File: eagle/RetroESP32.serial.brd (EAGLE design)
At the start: 71.2 x 115 mm, 70 parts, among them J1 AUDIO_JACK_3.5MM_KIT, J2 SPKR, J3 Batt Conn, J5 503182-1852_503182-1852, J6 USB4110-GF-A, Q3 DMG3415U-7, Q4 mmbt2222, Q5 mmbt2222, U1 ESP32-WROVER_ESP32-WROVER, U3 XC6210B332MR-G, U4 MCP73832T-2ACI/OT, U6 LM4875

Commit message: chore: pre indiegogo commit
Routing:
- net 3V3: track 299.7 -> 281.1 mm
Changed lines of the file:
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@@
 <drawing>
 <settings>
-<setting alwaysvectorfont="no"/>
+<setting alwaysvectorfont="yes"/>
 <setting verticaltext="up"/>
 </settings>
-<grid distance="1" unitdist="mm" unit="mm" style="lines" multiple="1" display="yes" altdistance="0.5" altunitdist="mm" altunit="mm"/>
+<grid distance="1" unitdist="mm" unit="mm" style="lines" multiple="1" display="yes" altdistance="0.05" altunitdist="mm" altunit="mm"/>
 <layers>
 <layer number="1" name="Top" color="4" fill="1" visible="yes" active="yes"/>
@@
 </layers>
 <board>
-<fusionsync huburn="a.cGVyc29uYWw6dWUyYjExYjI4" projecturn="a.cGVyc29uYWw6dWUyYjExYjI4IzIwMTkwNjA2MTk3NjIxNDMx" f3durn="urn:adsk.wipprod:dm.lineage:ZFl1xGfIQ26tyrlassmjWg" pcbguid="b66a3f17-6c90-49ae-b368-ab31643a6c6c" lastpulledtime="" lastsyncedchangeguid="1d1d8de5-610f-f58b-7720-f87a5a059bbd" latestrevisionid="" lastsyncedrevisionid="" lastboardhashguid="38cdb7cc-8c8c-2878-219a-16e2d022a318" lastpushedtime="2021-09-21T20:27:47Z" linktopcb3d="false"/>
 <fusionteam huburn="a.cGVyc29uYWw6dWUyYjExYjI4" projecturn="a.cGVyc29uYWw6dWUyYjExYjI4IzIwMTkwNjA2MTk3NjIxNDMx" folderUrn="urn:adsk.wipprod:fs.folder:co.pA_OyOrURcuKuaZfHTjB4g" urn="urn:adsk.wipprod:dm.lineage:ZdROvaXvSf-QMBwcavZMUg"  versionUrn="urn:adsk.wipprod:fs.file:vf.ZdROvaXvSf-QMBwcavZMUg?version=2" camFileUrn="urn:adsk.wipprod:dm.lineage:iU1Nsl3HQ2WKUaZAR9U5UA" camFileVersionUrn="urn:adsk.wipprod:fs.file:vf.iU1Nsl3HQ2WKUaZAR9U5UA?version=2" lastpublishedchangeguid="9850a083-763b-e2cf-a501-3ff3fee0d740"/>
 <plain>
@@
 <text x="2.1" y="31" size="1.016" layer="26" font="vector" ratio="20" rot="MR270" align="center">SCREW</text>
 <text x="2.1" y="27" size="1.4224" layer="26" font="vector" ratio="12" rot="SMR180" align="center">⇪</text>
-<polygon width="0" layer="21">
-<vertex x="0" y="52"/>
-<vertex x="0" y="1" curve="90"/>
-<vertex x="1" y="0"/>
-<vertex x="1" y="-0.5"/>
-<vertex x="17" y="-0.5"/>
-<vertex x="17" y="0"/>
-<vertex x="35" y="0" curve="90"/>
-<vertex x="35.5" y="0.5"/>
-<vertex x="35.5" y="1.75"/>
-<vertex x="42.5" y="1.75"/>
-<vertex x="42.5" y="0.5" curve="90"/>
-<vertex x="43" y="0"/>
-<vertex x="49.5" y="0" curve="90"/>
-<vertex x="50.5" y="1"/>
-<vertex x="50.5" y="16.95"/>
-<vertex x="68.5" y="16.95" curve="90"/>
-<vertex x="69.5" y="17.95"/>
-<vertex x="69.5" y="52"/>
-</polygon>
 <circle x="62" y="111" radius="1.25" width="0.4064" layer="26"/>
 <circle x="56.5" y="111" radius="1.25" width="0.4064" layer="26"/>
@@
 <wire x1="57.75" y1="92" x2="62" y2="92" width="0.6096" layer="16"/>
 <wire x1="34.75" y1="14.75" x2="34.75" y2="14.5" width="0.6096" layer="16"/>
-<wire x1="13" y1="12.75" x2="33" y2="12.75" width="0.6096" layer="16"/>
 <wire x1="34.75" y1="14.5" x2="33" y2="12.75" width="0.6096" layer="16"/>
 <wire x1="12.25" y1="71" x2="16" y2="71" width="0.6096" layer="16"/>
@@
 <wire x1="13.95" y1="30.075" x2="13.95" y2="31.95" width="0.6096" layer="1"/>
 <wire x1="13.95" y1="31.95" x2="14" y2="32" width="0.6096" layer="1"/>
-<wire x1="14" y1="32" x2="17" y2="32" width="0.6096" layer="1"/>
-<wire x1="17" y1="32" x2="17" y2="25.75" width="0.6096" layer="1"/>
-<wire x1="17" y1="25.75" x2="12.25" y2="21" width="0.6096" layer="1"/>
+<wire x1="14" y1="32" x2="18" y2="32" width="0.6096" layer="1"/>
+<wire x1="18" y1="32" x2="18" y2="26.75" width="0.6096" layer="1"/>
+<wire x1="18" y1="26.75" x2="12.25" y2="21" width="0.6096" layer="1"/>
 <wire x1="62" y1="111" x2="62" y2="100" width="0.6096" layer="16"/>
 <wire x1="12.25" y1="12.75" x2="12.25" y2="21" width="0.6096" layer="16"/>
@@
 <contactref element="U1" pad="VDD33"/>
 <contactref element="R6" pad="2"/>
+<wire x1="13" y1="12.75" x2="33" y2="12.75" width="0" layer="19" extent="16-16"/>
 </signal>
 <signal name="RESET">
@@
 <wire x1="20" y1="53.75" x2="21" y2="53.75" width="0.4064" layer="16"/>
 <wire x1="20" y1="49" x2="20" y2="53.75" width="0.4064" layer="16"/>
-<wire x1="20" y1="49" x2="20" y2="46" width="0.4064" layer="1"/>
-<wire x1="20" y1="46" x2="16" y2="42" width="0.4064" layer="1"/>
-<wire x1="15" y1="42" x2="16" y2="42" width="0.4064" layer="1"/>
+<wire x1="20" y1="49" x2="20" y2="45.9" width="0.4064" layer="1"/>
+<wire x1="20" y1="45.9" x2="16.1" y2="42" width="0.4064" layer="1"/>
+<wire x1="15" y1="42" x2="16.1" y2="42" width="0.4064" layer="1"/>
 <wire x1="13.94505" y1="43.55495" x2="13.95" y2="43.725" width="0.4064" layer="1"/>
 <wire x1="13.94505" y1="43.55495" x2="13.94505" y2="43.05495" width="0.4064" layer="1"/>
@@
 <via x="25" y="49.5" extent="1-16" drill="0.3"/>
 <wire x1="25" y1="52.25" x2="25" y2="49.5" width="0.4064" layer="16"/>
-<wire x1="25" y1="49" x2="25" y2="49.5" width="0.4064" layer="1"/>
+<wire x1="25" y1="49.1" x2="25" y2="49.5" width="0.4064" layer="1"/>
 <wire x1="19.025" y1="35.15" x2="18.85" y2="35.15" width="0.4064" layer="1"/>
 <wire x1="18.85" y1="35.15" x2="17" y2="37" width="0.4064" layer="1"/>
-<wire x1="17" y1="37" x2="17" y2="41" width="0.4064" layer="1"/>
-<wire x1="17" y1="41" x2="25" y2="49" width="0.4064" layer="1"/>
+<wire x1="17" y1="37" x2="17" y2="41.1" width="0.4064" layer="1"/>
+<wire x1="17" y1="41.1" x2="25" y2="49.1" width="0.4064" layer="1"/>
 </signal>
 <signal name="VOUT1">
@@
 </signals>
 <mfgpreviewcolors>
-<mfgpreviewcolor name="soldermaskcolor" color="0xC8FFFFFF"/>
+<mfgpreviewcolor name="soldermaskcolor" color="0xC8AA007F"/>
 <mfgpreviewcolor name="silkscreencolor" color="0xFF000000"/>
 <mfgpreviewcolor name="backgroundcolor" color="0xFF282828"/>
@@
 </note>
 <note version="8.3" severity="warning">
-Since Version 8.3, EAGLE supports Fusion synchronisation.
-This feature will not be available in this version and saving
-the document will break the link to the Fusion PCB feature.
-</note>
-<note version="8.3" severity="warning">

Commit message: feat: new button library
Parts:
- DOWN, LEFT, RIGHT, UP: value CONDUCTIVE_BUTTONCONDUCTIVE_BUTTON_DIRECTIONAL_THICK -> CONDUCTIVE_BUTTON; device RetroESP32:CONDUCTIVE_BUTTON_DIRECTIONAL_THICK -> RetroESP32:CONDUCTIVE_BUTTON_DIRECTIONAL
- J6: value USB4110-GF-A -> USB4105-GF-A; device USB4110-GF-A:GCT_USB4110-GF-A -> RetroESP32:GCT_USB4105-GF-A
- moved J6 3.50 mm to (1.50, 88.3)
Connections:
- net GND: now also J6.G1, J6.G2, J6.G3, J6.G4; no longer J6.S1, J6.S2, J6.S3, J6.S4
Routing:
- net 3V3: track 281.1 -> 301.4 mm
- net VBUS: track 46.4 -> 46.9 mm

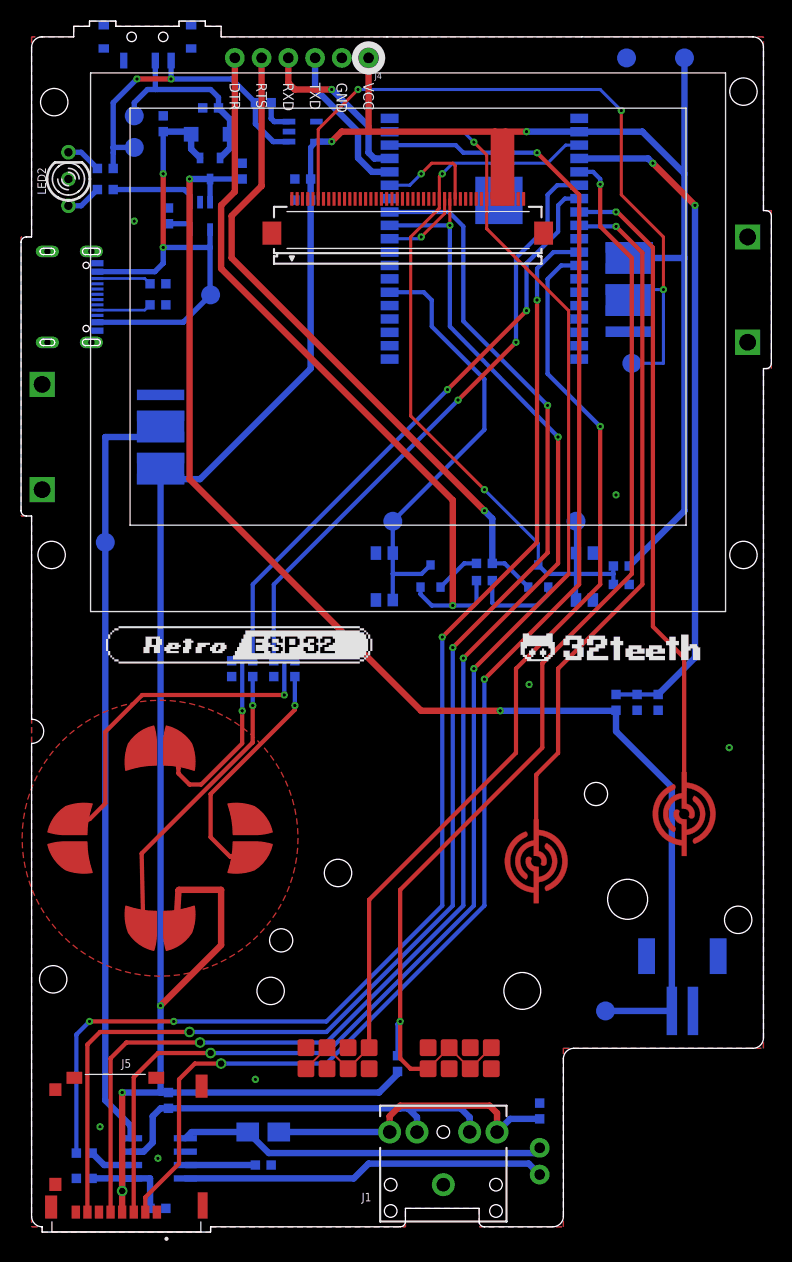
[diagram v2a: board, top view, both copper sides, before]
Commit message: feat: new A/B buttons, osh gerber
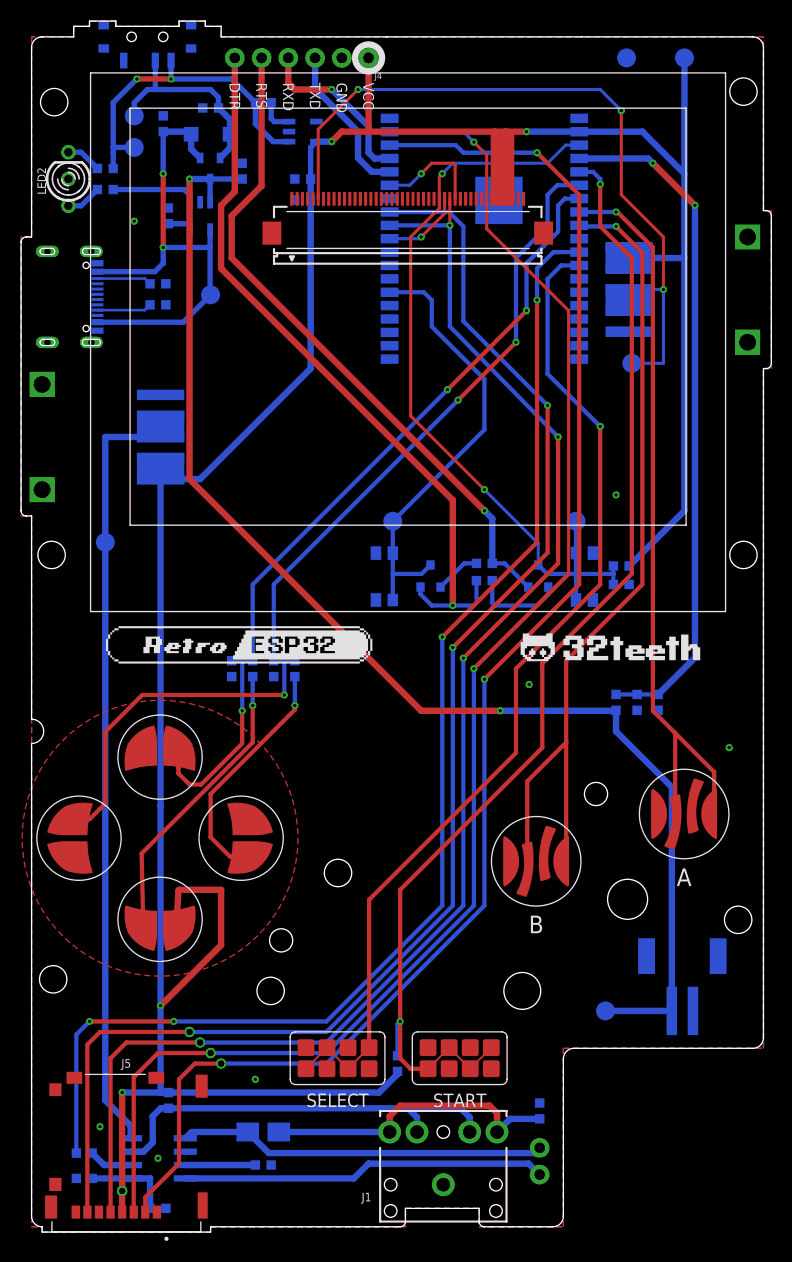
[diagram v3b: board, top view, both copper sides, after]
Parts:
- A, B: value CONDUCTIVE_BUTTONCONDUCTIVE_BUTTON_THICK -> CONDUCTIVE_BUTTONCONDUCTIVE_BUTTON_MGB; device RetroESP32:CONDUCTIVE_BUTTON_THICK -> RetroESP32:CONDUCTIVE_BUTTON_MGB
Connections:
- net GND: now also A.P$GND1, B.P$GND1
- net GPIO32: now also A.P$ACTIVE1
- net GPIO33: now also B.P$ACTIVE1
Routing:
- net GPIO33: track 66.8 -> 79.2 mm
- net GPIO32: track 61.2 -> 70.8 mm
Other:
- board text added: "A"
- board text added: "B"
- board text added: "SELECT"
- board text added: "START"
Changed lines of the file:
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@@
 <drawing>
 <settings>
-<setting alwaysvectorfont="yes"/>
+<setting alwaysvectorfont="no"/>
 <setting verticaltext="up"/>
 </settings>
@@
 <text x="21.84" y="109.35" size="1.016" layer="26" font="vector" ratio="20" rot="SMR270" align="center-left">RTS</text>
 <text x="19.3" y="109.35" size="1.016" layer="26" font="vector" ratio="20" rot="SMR270" align="center-left">DTR</text>
+<text x="47.92" y="28.71" size="1.6764" layer="25" font="vector" ratio="20" align="center">B</text>
+<text x="61.97" y="33.2" size="1.6764" layer="25" font="vector" ratio="20" align="center">A</text>
+<text x="40.655" y="12.01" size="1.27" layer="25" font="vector" ratio="20" align="center">START</text>
+<text x="29.055" y="12.01" size="1.27" layer="25" font="vector" ratio="20" align="center">SELECT</text>
 </plain>
 <attributes>
@@
 <attribute name="IGNORE_BOM" value="TRUE" x="29.055" y="16.01" size="1.778" layer="27" display="off"/>
 </element>
-<element name="B" library="RetroESP32" library_urn="urn:adsk.eagle:library:12566846" package="CONDUCTIVE_BUTTON_THICK" package3d_urn="urn:adsk.eagle:package:12566912/6" value="CONDUCTIVE_BUTTONCONDUCTIVE_BUTTON_THICK" x="47.92" y="34.71" smashed="yes" rot="R180">
+<element name="B" library="RetroESP32" library_urn="urn:adsk.eagle:library:12566846" package="CONDUCTIVE_BUTTON_MGB" value="CONDUCTIVE_BUTTONCONDUCTIVE_BUTTON_MGB" x="47.92" y="34.71" smashed="yes" rot="R180">
 <attribute name="IGNORE_BOM" value="TRUE" x="47.92" y="34.71" size="1.778" layer="27" rot="R180" display="off"/>
-</element>
-<element name="A" library="RetroESP32" library_urn="urn:adsk.eagle:library:12566846" package="CONDUCTIVE_BUTTON_THICK" package3d_urn="urn:adsk.eagle:package:12566912/6" value="CONDUCTIVE_BUTTONCONDUCTIVE_BUTTON_THICK" x="61.97" y="39.2" smashed="yes" rot="R180">
+<attribute name="SPICEPREFIX" value="B" x="47.92" y="34.71" size="1.778" layer="27" rot="R180" display="off"/>
+</element>
+<element name="A" library="RetroESP32" library_urn="urn:adsk.eagle:library:12566846" package="CONDUCTIVE_BUTTON_MGB" value="CONDUCTIVE_BUTTONCONDUCTIVE_BUTTON_MGB" x="61.97" y="39.2" smashed="yes" rot="R180">
 <attribute name="IGNORE_BOM" value="TRUE" x="61.97" y="39.2" size="1.778" layer="27" rot="R180" display="off"/>
 </element>
-<element name="UP" library="RetroESP32" library_urn="urn:adsk.eagle:library:12566846" package="CONDUCTIVE_BUTTON_DIRECTIONAL" value="CONDUCTIVE_BUTTON" x="12.2" y="44.6" smashed="yes" rot="R270">
+<element name="UP" library="RetroESP32" library_urn="urn:adsk.eagle:library:12566846" package="CONDUCTIVE_BUTTON_DIRECTIONAL" package3d_urn="urn:adsk.eagle:package:40166519/1" value="CONDUCTIVE_BUTTON" x="12.2" y="44.6" smashed="yes" rot="R270">
 <attribute name="IGNORE_BOM" value="TRUE" x="12.2" y="44.6" size="1.778" layer="27" rot="R270" display="off"/>
 </element>
-<element name="DOWN" library="RetroESP32" library_urn="urn:adsk.eagle:library:12566846" package="CONDUCTIVE_BUTTON_DIRECTIONAL" value="CONDUCTIVE_BUTTON" x="12.2" y="29.2" smashed="yes" rot="R90">
+<element name="DOWN" library="RetroESP32" library_urn="urn:adsk.eagle:library:12566846" package="CONDUCTIVE_BUTTON_DIRECTIONAL" package3d_urn="urn:adsk.eagle:package:40166519/1" value="CONDUCTIVE_BUTTON" x="12.2" y="29.2" smashed="yes" rot="R90">
 <attribute name="IGNORE_BOM" value="TRUE" x="12.2" y="29.2" size="1.778" layer="27" rot="R90" display="off"/>
 </element>
-<element name="LEFT" library="RetroESP32" library_urn="urn:adsk.eagle:library:12566846" package="CONDUCTIVE_BUTTON_DIRECTIONAL" value="CONDUCTIVE_BUTTON" x="4.5" y="36.9" smashed="yes">
+<element name="LEFT" library="RetroESP32" library_urn="urn:adsk.eagle:library:12566846" package="CONDUCTIVE_BUTTON_DIRECTIONAL" package3d_urn="urn:adsk.eagle:package:40166519/1" value="CONDUCTIVE_BUTTON" x="4.5" y="36.9" smashed="yes">
 <attribute name="IGNORE_BOM" value="TRUE" x="4.5" y="36.9" size="1.778" layer="27" display="off"/>
 </element>
-<element name="RIGHT" library="RetroESP32" library_urn="urn:adsk.eagle:library:12566846" package="CONDUCTIVE_BUTTON_DIRECTIONAL" value="CONDUCTIVE_BUTTON" x="19.9" y="36.9" smashed="yes" rot="R180">
+<element name="RIGHT" library="RetroESP32" library_urn="urn:adsk.eagle:library:12566846" package="CONDUCTIVE_BUTTON_DIRECTIONAL" package3d_urn="urn:adsk.eagle:package:40166519/1" value="CONDUCTIVE_BUTTON" x="19.9" y="36.9" smashed="yes" rot="R180">
 <attribute name="IGNORE_BOM" value="TRUE" x="19.9" y="36.9" size="1.778" layer="27" rot="R180" display="off"/>
 </element>
@@
 <contactref element="S1" pad="1"/>
 <contactref element="S1" pad="2"/>
+<contactref element="B" pad="P$GND1"/>
+<contactref element="A" pad="P$GND1"/>
 </signal>
 <signal name="3V3">
@@
 <wire x1="62" y1="111" x2="62" y2="100" width="0.6096" layer="16"/>
 <wire x1="12.25" y1="12.75" x2="12.25" y2="21" width="0.6096" layer="16"/>
-<wire x1="12.25" y1="21" x2="12.25" y2="71" width="0.6096" layer="16"/>
+<wire x1="12.25" y1="21" x2="12.25" y2="40" width="0.6096" layer="16"/>
+<wire x1="12.25" y1="40" x2="12.25" y2="71" width="0.6096" layer="16"/>
 <wire x1="8.6" y1="3.4" x2="8.6" y2="12.75" width="0.6096" layer="1"/>
 <via x="8.6" y="12.75" extent="1-16" drill="0.3"/>
@@
 <signal name="GPIO32">
 <contactref element="A" pad="P$ACTIVE"/>
-<wire x1="61.97" y1="41.45" x2="61.97" y2="54.03" width="0.4064" layer="1"/>
-<wire x1="61.97" y1="54.03" x2="59" y2="57" width="0.4064" layer="1"/>
 <via x="55.5" y="96.37" extent="1-16" drill="0.3"/>
 <wire x1="55.5" y1="96.37" x2="52" y2="96.37" width="0.4064" layer="16"/>
-<wire x1="59" y1="57" x2="59" y2="93" width="0.4064" layer="1"/>
-<wire x1="59" y1="93" x2="55.63" y2="96.37" width="0.4064" layer="1"/>
+<wire x1="59" y1="93" x2="59" y2="49" width="0.4064" layer="1"/>
+<wire x1="55.63" y1="96.37" x2="59" y2="93" width="0.4064" layer="1"/>
 <wire x1="55.63" y1="96.37" x2="55.5" y2="96.37" width="0.4064" layer="1"/>
 <contactref element="U1" pad="IO32"/>
+<contactref element="A" pad="P$ACTIVE1"/>
+<wire x1="64.82" y1="39.2" x2="64.82" y2="43.18" width="0.4064" layer="1"/>
+<wire x1="64.82" y1="43.18" x2="61.12" y2="46.88" width="0.4064" layer="1"/>
+<wire x1="61" y1="47" x2="59" y2="49" width="0.4064" layer="1"/>
+<wire x1="61.12" y1="46.88" x2="61" y2="47" width="0.4064" layer="1"/>
+<wire x1="61.12" y1="40.7" x2="61.12" y2="46.88" width="0.4064" layer="1"/>
 </signal>
 <signal name="GPIO33">
 <contactref element="B" pad="P$ACTIVE"/>
-<wire x1="47.92" y1="36.96" x2="47.92" y2="42.92" width="0.4064" layer="1"/>
-<wire x1="47.92" y1="42.92" x2="50" y2="45" width="0.4064" layer="1"/>
-<wire x1="50" y1="45" x2="50" y2="53" width="0.4064" layer="1"/>
-<wire x1="50" y1="53" x2="58" y2="61" width="0.4064" layer="1"/>
 <via x="55.5" y="95" extent="1-16" drill="0.3"/>
 <wire x1="55.5" y1="95" x2="52.1" y2="95" width="0.4064" layer="16"/>
 <wire x1="52.1" y1="95" x2="52" y2="95.1" width="0.4064" layer="16"/>
-<wire x1="58" y1="61" x2="58" y2="92.5" width="0.4064" layer="1"/>
+<wire x1="58" y1="92.5" x2="58" y2="61" width="0.4064" layer="1"/>
 <wire x1="58" y1="92.5" x2="55.5" y2="95" width="0.4064" layer="1"/>
 <contactref element="U1" pad="IO33"/>
+<contactref element="B" pad="P$ACTIVE1"/>
+<wire x1="58" y1="61" x2="50.77" y2="53.77" width="0.4064" layer="1"/>
+<wire x1="50.77" y1="53.77" x2="50.77" y2="46" width="0.4064" layer="1"/>
+<wire x1="50.77" y1="46" x2="50.77" y2="34.71" width="0.4064" layer="1"/>
+<wire x1="47.07" y1="42.3" x2="50.77" y2="46" width="0.4064" layer="1"/>
+<wire x1="47.07" y1="36.21" x2="47.07" y2="42.3" width="0.4064" layer="1"/>
 </signal>
 <signal name="GPIO35">
@@
 </signals>
 <mfgpreviewcolors>
-<mfgpreviewcolor name="soldermaskcolor" color="0xC8005500"/>
+<mfgpreviewcolor name="soldermaskcolor" color="0xC8AA00FF"/>
 <mfgpreviewcolor name="silkscreencolor" color="0xFFFFFFFF"/>
 <mfgpreviewcolor name="backgroundcolor" color="0xFF282828"/>
